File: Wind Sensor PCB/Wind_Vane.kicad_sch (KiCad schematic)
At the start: 7 parts, among them U1 TSV911xxLx

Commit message: Large update - firmware and PCB design. V2
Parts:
- D1: value 5V1_Zener -> 3V3_Zener; LCSC C131770 -> C493206
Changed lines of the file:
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@@
 			)
 		)
-		(property "Value" "5V1_Zener"
+		(property "Value" "3V3_Zener"
 			(at 108.4326 101.473 90)
 			(effects
@@
 			)
 		)
-		(property "LCSC" "C131770"
+		(property "LCSC" " C493206"
 			(at 106.68 100.33 0)
 			(effects
@@
 			(at 106.68 100.33 0)
 			(effects
+				(font
+					(size 1.27 1.27)
+				)
+				(hide yes)
+			)
+		)
+		(property "Supplier 1" ""
+			(at 106.68 100.33 0)
+			(effects
+				(font
+					(size 1.27 1.27)
+				)
+				(hide yes)
+			)
+		)
+		(property "Supplier 1 Code" ""
+			(at 106.68 100.33 0)
+			(effects
+				(font
+					(size 1.27 1.27)
+				)
+				(hide yes)
+			)
+		)
+		(property "Supplier 1 Web" ""
+			(at 106.68 100.33 0)
+			(effects
+				(font
+					(size 1.27 1.27)
+				)
+				(hide yes)
+			)
+		)
+		(property "Supplier 2" ""
+			(at 106.68 100.33 0)
+			(effects
+				(font
+					(size 1.27 1.27)
+				)
+				(hide yes)
+			)
+		)
+		(property "Supplier 2 Code" ""
+			(at 106.68 100.33 0)
+			(effects
+				(font
+					(size 1.27 1.27)
+				)
+				(hide yes)
+			)
+		)
+		(property "Supplier 2 Web" ""
+			(at 106.68 100.33 0)
+			(effects
+				(font
+					(size 1.27 1.27)
+				)
+				(hide yes)
+			)
+		)
+		(property "Manufacturer" ""
+			(at 106.68 100.33 0)
+			(effects
+				(font
+					(size 1.27 1.27)
+				)
+				(hide yes)
+			)
+		)
+		(property "Manufacturer Part" ""
+			(at 106.68 100.33 0)
+			(effects
+				(font
+					(size 1.27 1.27)
+				)
+				(hide yes)
+			)
+		)
+		(property "Supplier 1 Cost" ""
+			(at 106.68 100.33 0)
+			(effects
+				(font
+					(size 1.27 1.27)
+				)
+				(hide yes)
+			)
+		)
+		(property "Supplier 2 Cost" ""
+			(at 106.68 100.33 0)
+			(effects
+				(font
+					(size 1.27 1.27)
+				)
+				(hide yes)
+			)
+		)
+		(property "JLCPCB Cost" ""
+			(at 106.68 100.33 0)
+			(effects

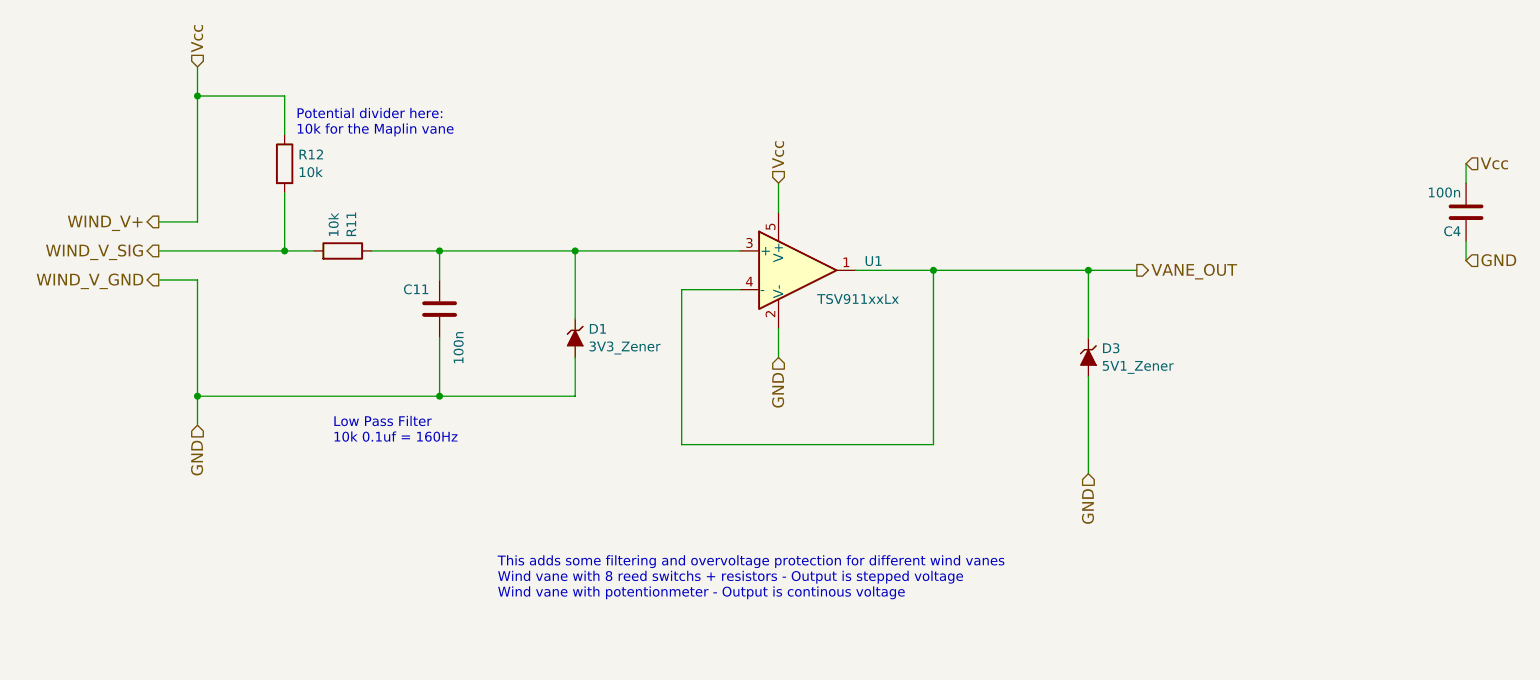
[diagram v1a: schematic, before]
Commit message: updated wind vane input
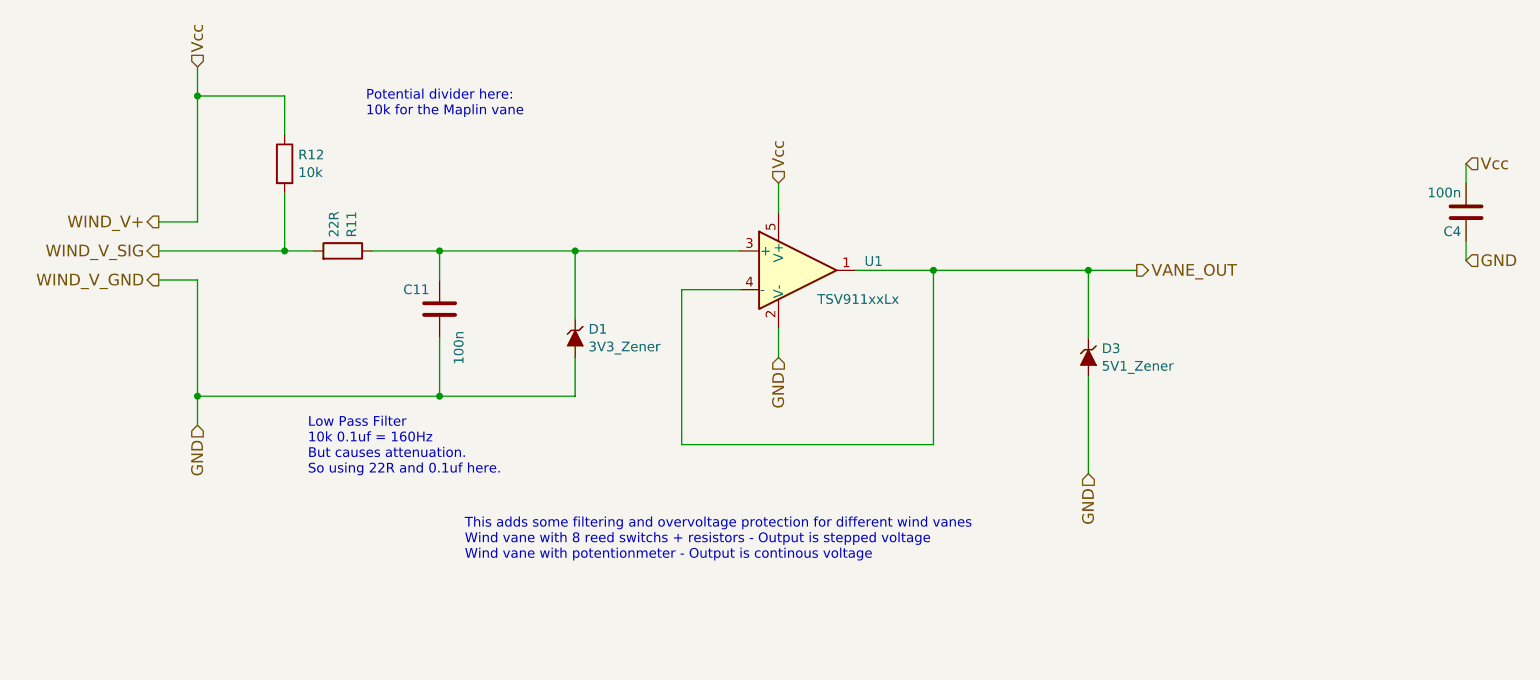
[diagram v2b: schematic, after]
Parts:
- R11: value 10k -> 22R; LCSC C17414 -> C25295; Manufacturer Part MCMR08X1002FTL -> 0805W8J0220T5E
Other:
- note added: "Low Pass Filter 10k 0.1uf = 160Hz But causes attenuation. So using 22R and 0.1uf here."
- note removed: "Low Pass Filter 10k 0.1uf = 160Hz"
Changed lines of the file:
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@@
 	(text "This adds some filtering and overvoltage protection for different wind vanes\nWind vane with 8 reed switchs + resistors - Output is stepped voltage\nWind vane with potentionmeter - Output is continous voltage"
 		(exclude_from_sim no)
-		(at 96.52 134.62 0)
+		(at 92.202 129.54 0)
 		(effects
 			(font
@@
 		)
 	)
-	(text "Low Pass Filter\n10k 0.1uf = 160Hz"
+	(text "Low Pass Filter\n10k 0.1uf = 160Hz\nBut causes attenuation.\nSo using 22R and 0.1uf here."
 		(exclude_from_sim no)
-		(at 74.93 114.3 0)
+		(at 71.628 118.364 0)
 		(effects
 			(font
@@
 	(text "Potential divider here:\n10k for the Maplin vane"
 		(exclude_from_sim no)
-		(at 70.104 73.914 0)
+		(at 79.248 71.374 0)
 		(effects
 			(font
@@
 			)
 		)
-		(property "Value" "10k"
+		(property "Value" "22R"
 			(at 75.057 87.122 0)
 			(effects
@@
 			)
 		)
-		(property "Manufacturer Part" "MCMR08X1002FTL"
+		(property "Manufacturer Part" "0805W8J0220T5E"
 			(at 76.2 88.9 0)
 			(effects
@@
 			)
 		)
-		(property "LCSC" "C17414"
+		(property "LCSC" "C25295"
 			(at 76.2 88.9 0)
 			(effects

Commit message: Changed to 5V6 zener on all protection
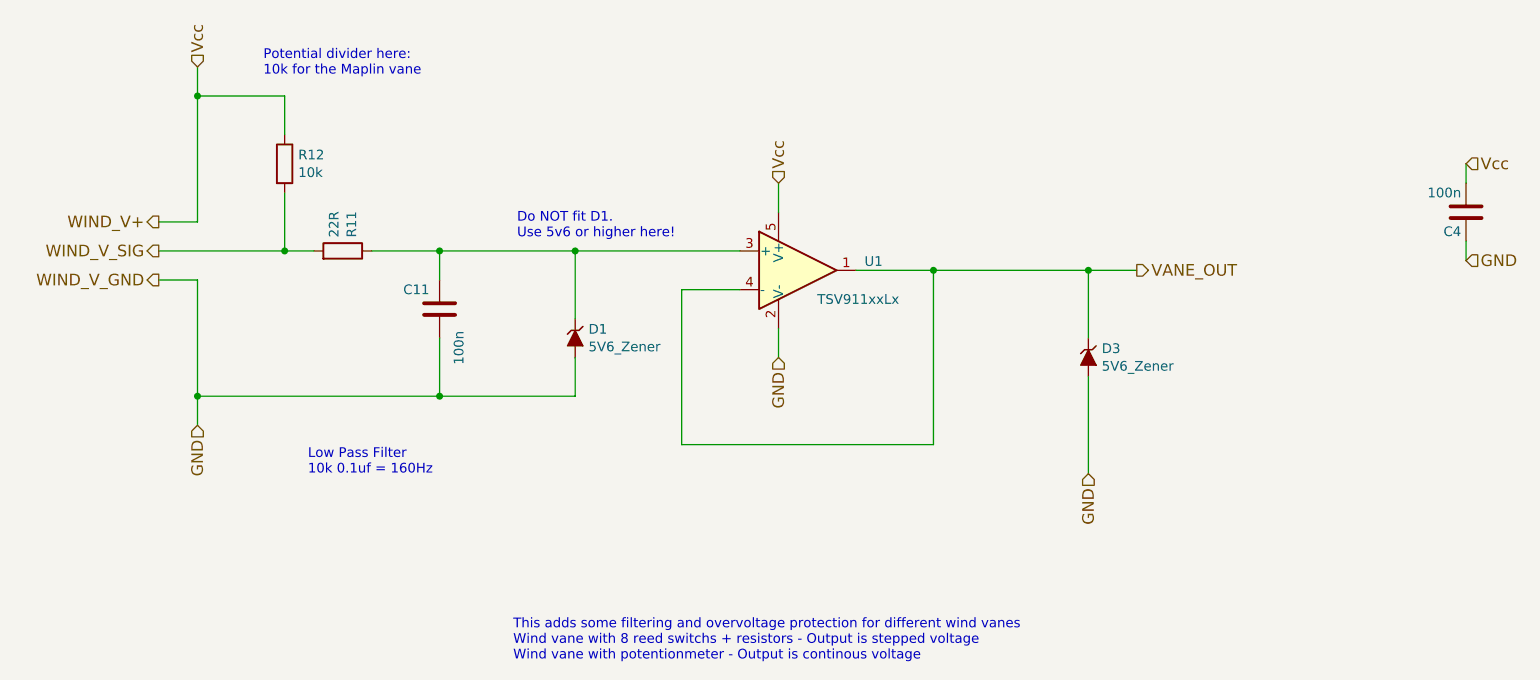
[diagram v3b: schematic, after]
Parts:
- D1: value 3V3_Zener -> 5V6_Zener; LCSC C493206 -> C213355
- D3: value 5V1_Zener -> 5V6_Zener; LCSC C131770 -> C213355
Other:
- note added: "Do NOT fit D1. Use 5v6 or higher here!"
- note added: "Low Pass Filter 10k 0.1uf = 160Hz"
- note removed: "Low Pass Filter 10k 0.1uf = 160Hz But causes attenuation. So using 22R and 0.1uf here."
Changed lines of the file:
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@@
+		)
+	)
+	(text "Do NOT fit D1.\nUse 5v6 or higher here!"
+		(exclude_from_sim no)
+		(at 99.06 87.376 0)
+		(effects
+			(font
+				(size 1.27 1.27)
+			)
+			(justify left bottom)
 		)
 	)
 	(text "This adds some filtering and overvoltage protection for different wind vanes\nWind vane with 8 reed switchs + resistors - Output is stepped voltage\nWind vane with potentionmeter - Output is continous voltage"
 		(exclude_from_sim no)
-		(at 92.202 129.54 0)
+		(at 98.552 142.748 0)
 		(effects
 			(font
@@
 		)
 	)
-	(text "Low Pass Filter\n10k 0.1uf = 160Hz\nBut causes attenuation.\nSo using 22R and 0.1uf here."
+	(text "Low Pass Filter\n10k 0.1uf = 160Hz\n"
 		(exclude_from_sim no)
 		(at 71.628 118.364 0)
@@
 	(text "Potential divider here:\n10k for the Maplin vane"
 		(exclude_from_sim no)
-		(at 79.248 71.374 0)
+		(at 65.786 66.04 0)
 		(effects
 			(font
@@
 			)
 		)
-		(property "Value" "3V3_Zener"
+		(property "Value" "5V6_Zener"
 			(at 108.4326 101.473 90)
 			(effects
@@
 			)
 		)
-		(property "LCSC" " C493206"
+		(property "LCSC" " C213355"
 			(at 106.68 100.33 0)
 			(effects
@@
 			)
 		)
-		(property "Value" "5V1_Zener"
+		(property "Value" "5V6_Zener"
 			(at 175.7426 104.013 90)
 			(effects
@@
 			)
 		)
-		(property "LCSC" "C131770"
+		(property "LCSC" " C213355"
 			(at 173.99 102.87 0)
 			(effects
@@
 			(at 173.99 102.87 0)
 			(effects
+				(font
+					(size 1.27 1.27)
+				)
+				(hide yes)
+			)
+		)
+		(property "Supplier 1" ""
+			(at 173.99 102.87 0)
+			(effects
+				(font
+					(size 1.27 1.27)
+				)
+				(hide yes)
+			)
+		)
+		(property "Supplier 1 Code" ""
+			(at 173.99 102.87 0)
+			(effects
+				(font
+					(size 1.27 1.27)
+				)
+				(hide yes)
+			)
+		)
+		(property "Supplier 1 Web" ""
+			(at 173.99 102.87 0)
+			(effects
+				(font
+					(size 1.27 1.27)
+				)
+				(hide yes)
+			)
+		)
+		(property "Supplier 2" ""
+			(at 173.99 102.87 0)
+			(effects
+				(font
+					(size 1.27 1.27)
+				)
+				(hide yes)
+			)
+		)
+		(property "Supplier 2 Code" ""
+			(at 173.99 102.87 0)
+			(effects
+				(font
+					(size 1.27 1.27)
+				)
+				(hide yes)
+			)
+		)
+		(property "Supplier 2 Web" ""
+			(at 173.99 102.87 0)
+			(effects
+				(font
+					(size 1.27 1.27)
+				)
+				(hide yes)
+			)
+		)
+		(property "Manufacturer" ""
+			(at 173.99 102.87 0)
+			(effects
+				(font
+					(size 1.27 1.27)
+				)
+				(hide yes)
+			)
+		)
+		(property "Manufacturer Part" ""
+			(at 173.99 102.87 0)
+			(effects
+				(font
+					(size 1.27 1.27)
+				)
+				(hide yes)
+			)
+		)
+		(property "Supplier 1 Cost" ""
+			(at 173.99 102.87 0)
+			(effects
+				(font
+					(size 1.27 1.27)
+				)
+				(hide yes)
+			)
+		)
+		(property "Supplier 2 Cost" ""
+			(at 173.99 102.87 0)
+			(effects
+				(font
+					(size 1.27 1.27)
+				)
+				(hide yes)
+			)
+		)
+		(property "JLCPCB Cost" ""
+			(at 173.99 102.87 0)
+			(effects

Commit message: updated instructions and schematic files
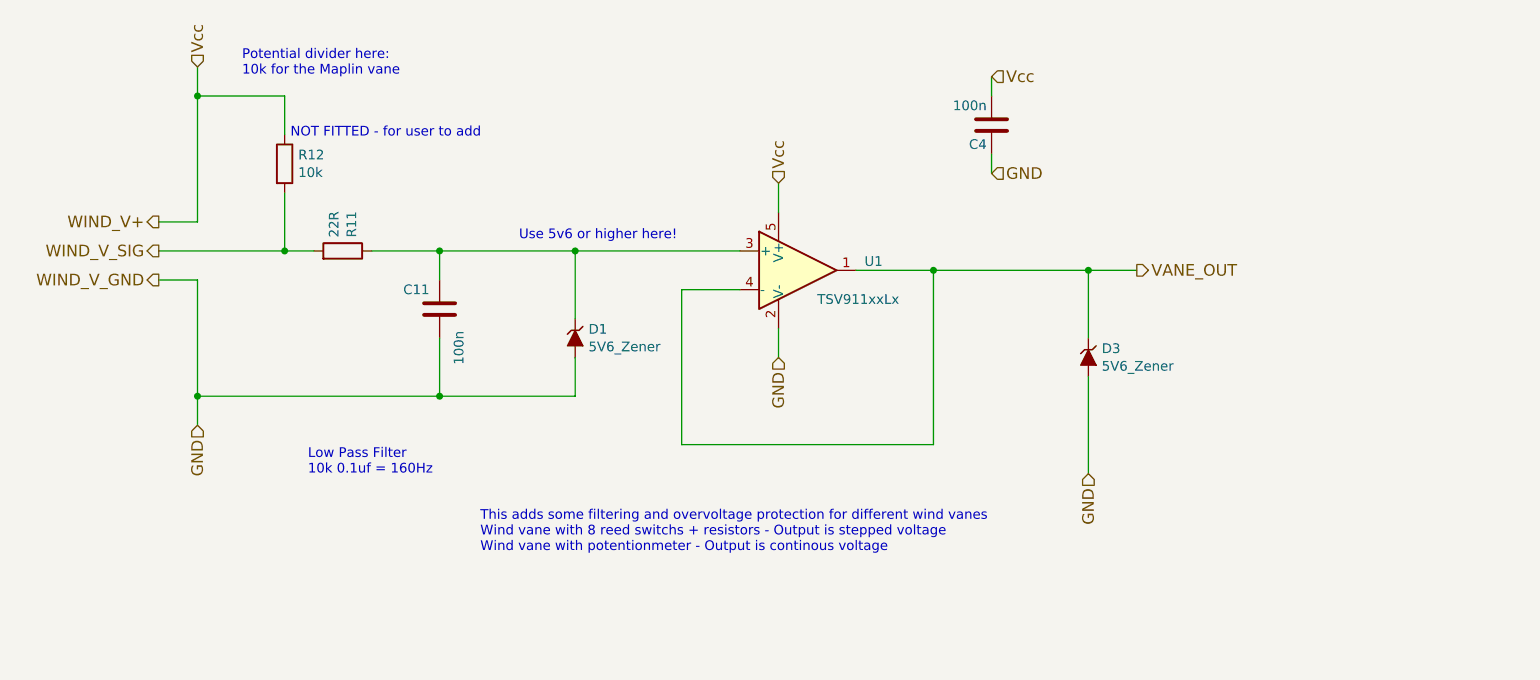
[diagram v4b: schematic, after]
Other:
- note added: "NOT FITTED - for user to add"
- note added: "Use 5v6 or higher here!"
- note removed: "Do NOT fit D1. Use 5v6 or higher here!"
- moved on the sheet: C4
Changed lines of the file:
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@@
 	(wire
 		(pts
-			(xy 223.52 90.17) (xy 223.52 87.63)
+			(xy 161.29 78.74) (xy 161.29 76.2)
 		)
 		(stroke
@@
 	(wire
 		(pts
-			(xy 223.52 80.01) (xy 223.52 77.47)
+			(xy 161.29 68.58) (xy 161.29 66.04)
 		)
 		(stroke
@@
 		)
 	)
-	(text "Do NOT fit D1.\nUse 5v6 or higher here!"
-		(exclude_from_sim no)
-		(at 99.06 87.376 0)
+	(text "NOT FITTED - for user to add"
+		(exclude_from_sim no)
+		(at 69.342 74.168 0)
 		(effects
 			(font
@@
 		)
 	)
+	(text "Use 5v6 or higher here!"
+		(exclude_from_sim no)
+		(at 99.314 87.63 0)
+		(effects
+			(font
+				(size 1.27 1.27)
+			)
+			(justify left bottom)
+		)
+	)
 	(text "This adds some filtering and overvoltage protection for different wind vanes\nWind vane with 8 reed switchs + resistors - Output is stepped voltage\nWind vane with potentionmeter - Output is continous voltage"
 		(exclude_from_sim no)
-		(at 98.552 142.748 0)
+		(at 94.234 128.524 0)
 		(effects
 			(font
@@
 	(text "Potential divider here:\n10k for the Maplin vane"
 		(exclude_from_sim no)
-		(at 65.786 66.04 0)
+		(at 62.992 66.04 0)
 		(effects
 			(font
@@
 	(hierarchical_label "GND"
 		(shape input)
-		(at 223.52 90.17 0)
+		(at 161.29 78.74 0)
 		(fields_autoplaced yes)
 		(effects
@@
 	(hierarchical_label "Vcc"
 		(shape input)
-		(at 223.52 77.47 0)
+		(at 161.29 66.04 0)
 		(fields_autoplaced yes)
 		(effects
@@
 	(symbol
 		(lib_id "device:C")
-		(at 223.52 83.82 180)
+		(at 161.29 72.39 180)
 		(unit 1)
 		(exclude_from_sim no)
@@
 		(dnp no)
 		(property "Reference" "C4"
-			(at 222.885 86.36 0)
+			(at 160.655 74.93 0)
 			(effects
 				(font
@@
 		)
 		(property "Value" "100n"
-			(at 222.885 81.28 0)
+			(at 160.655 69.85 0)
 			(effects
 				(font
@@
 		)
 		(property "Footprint" "REInnovationFootprint:SM_C_0805"
-			(at 222.5548 80.01 0)
+			(at 160.3248 68.58 0)
 			(effects
 				(font
@@
 		)
 		(property "Datasheet" ""
-			(at 223.52 83.82 0)
+			(at 161.29 72.39 0)
 			(effects
 				(font
@@
 		)
 		(property "Description" ""
-			(at 223.52 83.82 0)
+			(at 161.29 72.39 0)
 			(effects
 				(font
@@
 		)
 		(property "LCSC" "C49678"
-			(at 223.52 83.82 0)
+			(at 161.29 72.39 0)
 			(effects
 				(font
@@
 		)
 		(property "JLCPCB Add" "Y"
-			(at 223.52 83.82 0)
+			(at 161.29 72.39 0)
 			(effects
 				(font
@@
 		)
 		(property "JLCPCB Cost" "0.0108"
-			(at 223.52 83.82 0)
-			(effects
-				(font
+			(at 161.29 72.39 0)
+			(effects
+				(font
